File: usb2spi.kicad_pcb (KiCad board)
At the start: 2 copper layers, 15 parts, among them J1 Vout 3.3v 50mA, J2 SPI, J3 Additional, J4 GPIO, J5 Suspend

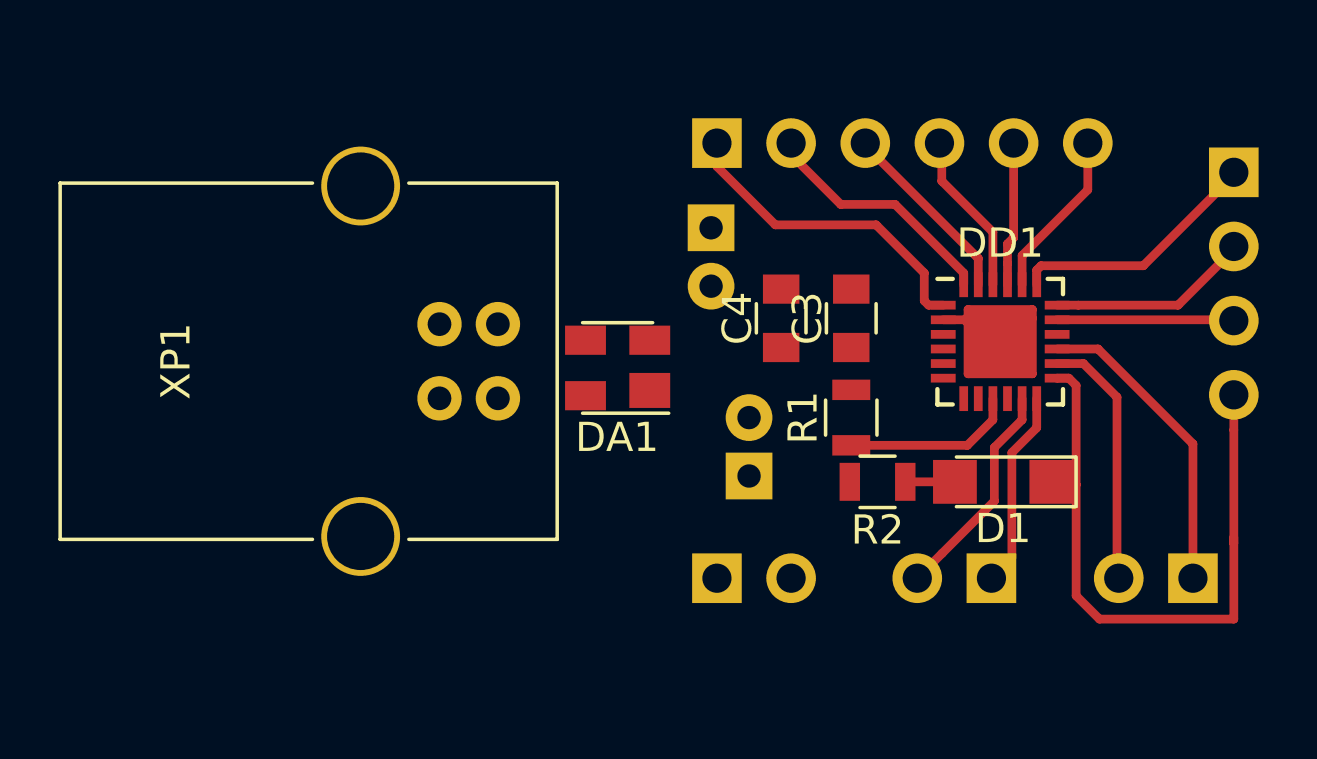
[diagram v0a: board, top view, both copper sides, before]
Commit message: Trace PCB
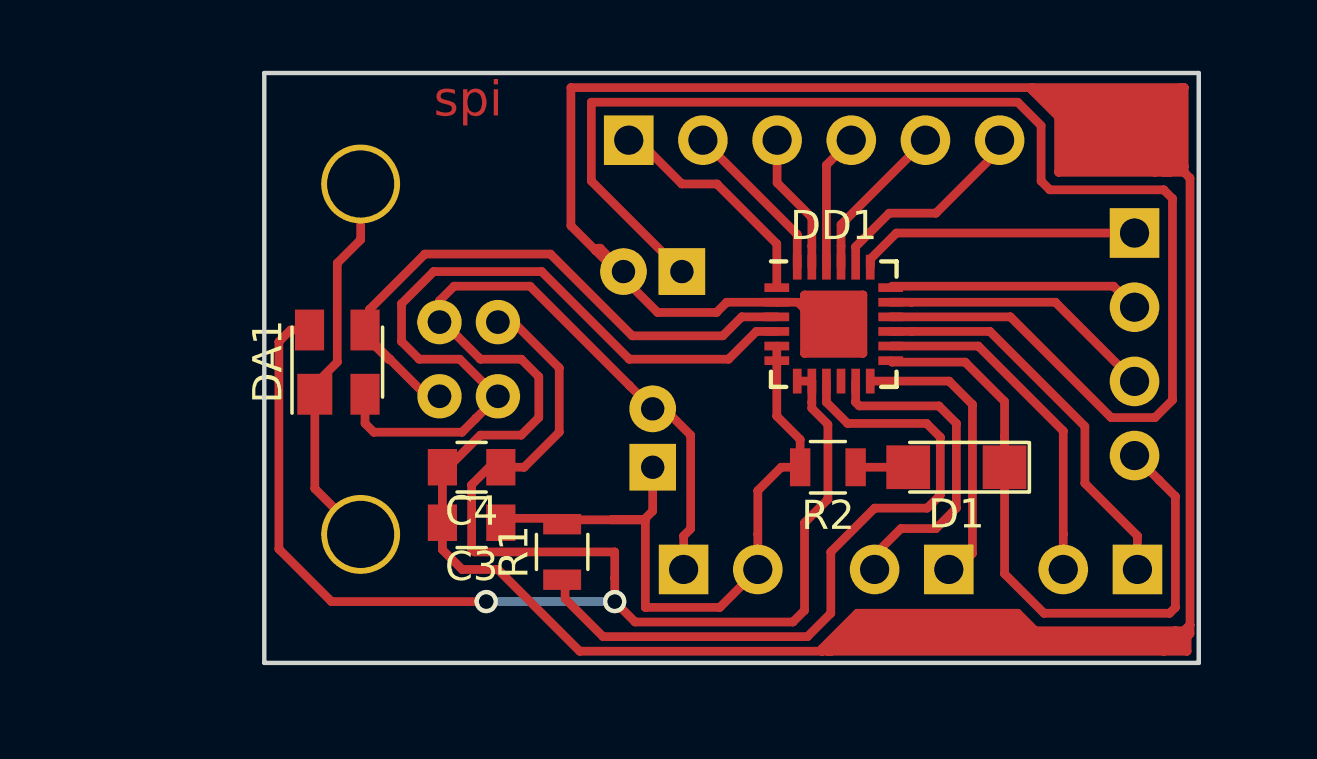
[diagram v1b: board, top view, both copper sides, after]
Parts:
- XP1: moved to B.Cu
- moved C3 14.8 mm to (125.6, 72.9), turned to 180 degrees
- moved C4 11.8 mm to (125.6, 71.0), turned to 180 degrees
- moved R1 10.9 mm to (128.7, 73.9)
- moved DA1 9.60 mm to (121.0, 67.4), turned to 90 degrees
- moved DD1 5.73 mm to (138.0, 66.1)
- moved J3 3.99 mm to (148.3, 63.0)
- moved C2 3.31 mm to (131.8, 71.0)
- moved J2 3.02 mm to (131.0, 59.8)
- moved XP1 2.61 mm to (126.5, 66.0)
- moved J4 1.92 mm to (148.4, 74.5)
- moved C1 1.80 mm to (132.8, 64.3), turned to 180 degrees
- moved R2 1.77 mm to (137.8, 71.0)
- moved D1 1.68 mm to (142.2, 71.0)
- moved J5 1.49 mm to (141.9, 74.5)
- moved J1 1.18 mm to (132.9, 74.5)
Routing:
- net Net-(C1-Pad2): track 39.1 -> 261.2 mm
- net Net-(C4-Pad1): track 0.00 -> 54.4 mm, vias 0 -> 2
- net Net-(C1-Pad1): track 0.00 -> 47.8 mm
- net Net-(DA1-Pad2): track 0.00 -> 26.6 mm
- net Net-(C2-Pad1): track 0.00 -> 24.3 mm
- net Net-(DA1-Pad3): track 0.00 -> 21.9 mm
- net Net-(DD1-Pad9): track 5.94 -> 24.4 mm
- net Net-(DA1-Pad1): track 0.00 -> 13.3 mm
- net Net-(DD1-Pad11): track 7.64 -> 11.3 mm
- net Net-(DD1-Pad17): track 6.16 -> 9.47 mm
- net Net-(DD1-Pad12): track 6.79 -> 9.97 mm
- net Net-(DD1-Pad14): track 8.78 -> 11.9 mm
- net Net-(DD1-Pad15): track 10.6 -> 13.6 mm
- net Net-(DD1-Pad1): track 10.7 -> 8.04 mm
- net Net-(DD1-Pad24): track 7.99 -> 5.69 mm
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- added copper zone on F.Cu, net Net-(C1-Pad2)
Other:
- board outline added: 32 x 20.2 mm
- board text added: "spi"

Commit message: Fix PCB
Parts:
- moved C1 9.84 mm to (142.6, 65.2), turned to 0 degrees
- moved D1 1.02 mm to (141.2, 71.2)
- moved R2 1.02 mm to (136.8, 71.2)
- moved C2 0.20 mm to (131.8, 71.2)
- moved C4 0.20 mm to (125.6, 71.2)
- moved DD1 0.20 mm to (138.0, 66.3)
- moved J1 0.20 mm to (132.9, 74.7)
- moved J2 0.20 mm to (131.0, 60.0)
- moved J3 0.20 mm to (148.3, 63.2)
- moved J4 0.20 mm to (148.4, 74.7)
- moved J5 0.20 mm to (141.9, 74.7)
- moved XP1 0.20 mm to (126.5, 66.2)
- moved C3 0.20 mm to (125.6, 73.1)
- moved DA1 0.20 mm to (121.0, 67.6)
- moved R1 0.20 mm to (128.7, 74.1)
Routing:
- net Net-(C1-Pad2): track 261.2 -> 205.1 mm
- net Net-(C1-Pad1): track 47.8 -> 2.20 mm
- net Net-(C2-Pad1): track 24.3 -> 32.8 mm
- net Net-(DD1-Pad17): track 9.47 -> 12.6 mm
- net Net-(DD1-Pad18): track 8.67 -> 10.9 mm
- net Net-(DD1-Pad11): track 11.3 -> 9.49 mm
- net Net-(DD1-Pad9): track 24.4 -> 23.0 mm
- net Net-(DA1-Pad3): track 21.9 -> 20.7 mm
- net Net-(DD1-Pad12): track 9.97 -> 8.77 mm
- net Net-(C4-Pad1): track 54.4 -> 53.3 mm
- net Net-(DD1-Pad1): track 8.04 -> 7.30 mm
- net Net-(DD1-Pad19): track 9.70 -> 10.4 mm
- net Net-(DA1-Pad1): track 13.3 -> 14.0 mm
- net Net-(DA1-Pad2): track 26.6 -> 26.0 mm
- net Net-(DD1-Pad15): track 13.6 -> 14.2 mm
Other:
- board size 32 x 20.2 mm -> 32.5 x 20.5 mm
- net class Default: clearance 0.2 -> 0.25; trace_width 0.3 -> 0.2; via_drill 0.5 -> 0.7
- rule trace_clearance: 0.2 -> 0.25
- rule trace_min: 0.25 -> 0.2
